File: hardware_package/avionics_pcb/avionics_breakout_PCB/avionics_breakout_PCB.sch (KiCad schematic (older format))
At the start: 5 parts, among them SW1 SW_Push

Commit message: Completed the PCB for the breakout board based avionics board. Also updated the CI/CD to include this new PCB
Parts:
- added J1: GPS, Connector_PinHeader_2.54mm:PinHeader_1x04_P2.54mm_Vertical, symbol Connector_Generic:Conn_01x04
- Barometer1: symbol avionics:MPL3115A2-Adafruit -> avionics_breakout_PCB-rescue:MPL3115A2-Adafruit-avionics
- IMU1: symbol avionics:MPU-6050-Adafruit -> avionics_breakout_PCB-rescue:MPU-6050-Adafruit-avionics
- LoRa_Radio1: symbol avionics:RFM98 -> avionics_breakout_PCB-rescue:RFM98-avionics
- STM32: symbol avionics:Adafruit_Feather_STM32F405 -> avionics_breakout_PCB-rescue:Adafruit_Feather_STM32F405-avionics
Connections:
- net GND: now also IMU1.7 (GND), LoRa_Radio1.16 (GND), LoRa_Radio1.2 (GND), LoRa_Radio1.9 (GND), J1.2 (Pin_2); no longer LoRa_Radio1.10 (GND)
- net CS: now reaches STM32.10 (A5)
- net CS: now also LoRa_Radio1.12 (NSS)
- net SCK: now reaches STM32.11 (SCK)
- net SCK: now also LoRa_Radio1.13 (SCK)
- net MOSI: now reaches STM32.12 (MO)
- net MOSI: now also LoRa_Radio1.14 (MOSI)
- net MISO: now reaches STM32.13 (MI)
- net MISO: now also LoRa_Radio1.15 (MISO)
- net RX: now reaches STM32.14 (RX)
- net RX: now also J1.4 (Pin_4)
- net TX: now reaches STM32.15 (TX)
- net TX: now also J1.3 (Pin_3)
- net INT_IMU: now reaches STM32.19 (5)
- net INT_IMU: now also IMU1.6 (INT)
- net RESET: now reaches STM32.20 (6)
- net RESET: now also LoRa_Radio1.11 (RESET)
- net INT_LORA: now reaches STM32.21 (9)
- net INT_LORA: now also LoRa_Radio1.6 (DIO0)
- net +3V3: now reaches LoRa_Radio1.5 (3V3)
- net +3V3: now also Barometer1.1 (VIN), IMU1.1 (VCC), STM32.2 (3V3), SW1.2, J1.1 (Pin_1)
- removed net 3V3: Barometer1.1 (VIN), IMU1.1 (VCC), LoRa_Radio1.13 (3V3), STM32.2 (3V3), STM32.3 (3V3), SW1.2
- no-connect marks 4 -> 29
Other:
- moved on the sheet: Barometer1, STM32, SW1

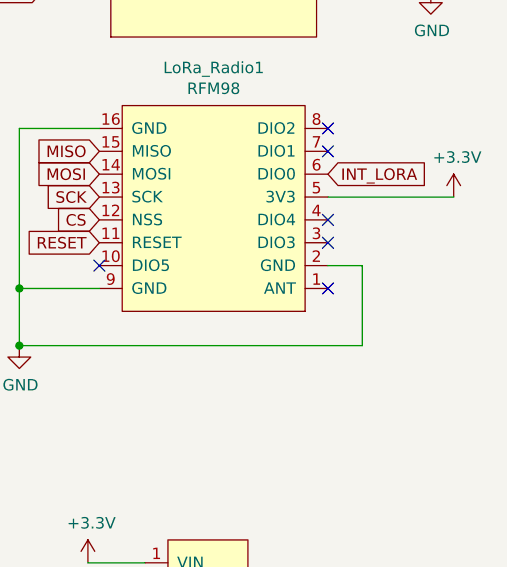
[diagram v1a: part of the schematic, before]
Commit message: Fixed DRC check errors
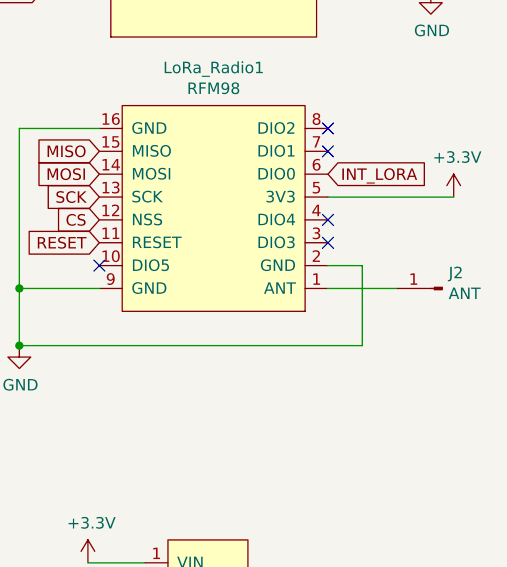
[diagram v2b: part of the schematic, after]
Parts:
- added J2: ANT, Connector_Wire:SolderWire-0.1sqmm_1x01_D0.4mm_OD1mm, symbol Connector:Conn_01x01_Male
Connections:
- net at LoRa_Radio1.1 (ANT): now also J2.1 (Pin_1)
- no-connect marks 29 -> 28
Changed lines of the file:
@@
 Wire Wire Line
 	8500 1500 8300 1500
-NoConn ~ 8050 2800
+$Comp
+L Connector:Conn_01x01_Male J2
+U 1 1 5F636A13
+P 8550 2800
+F 0 "J2" H 8522 2732 50  0000 R CNN
+F 1 "ANT" H 8522 2823 50  0000 R CNN
+F 2 "Connector_Wire:SolderWire-0.1sqmm_1x01_D0.4mm_OD1mm" H 8550 2800 50  0001 C CNN
+F 3 "~" H 8550 2800 50  0001 C CNN
+	1    8550 2800
+	-1   0    0    1
+$EndComp
+Wire Wire Line
+	8050 2800 8350 2800
 $EndSCHEMATC

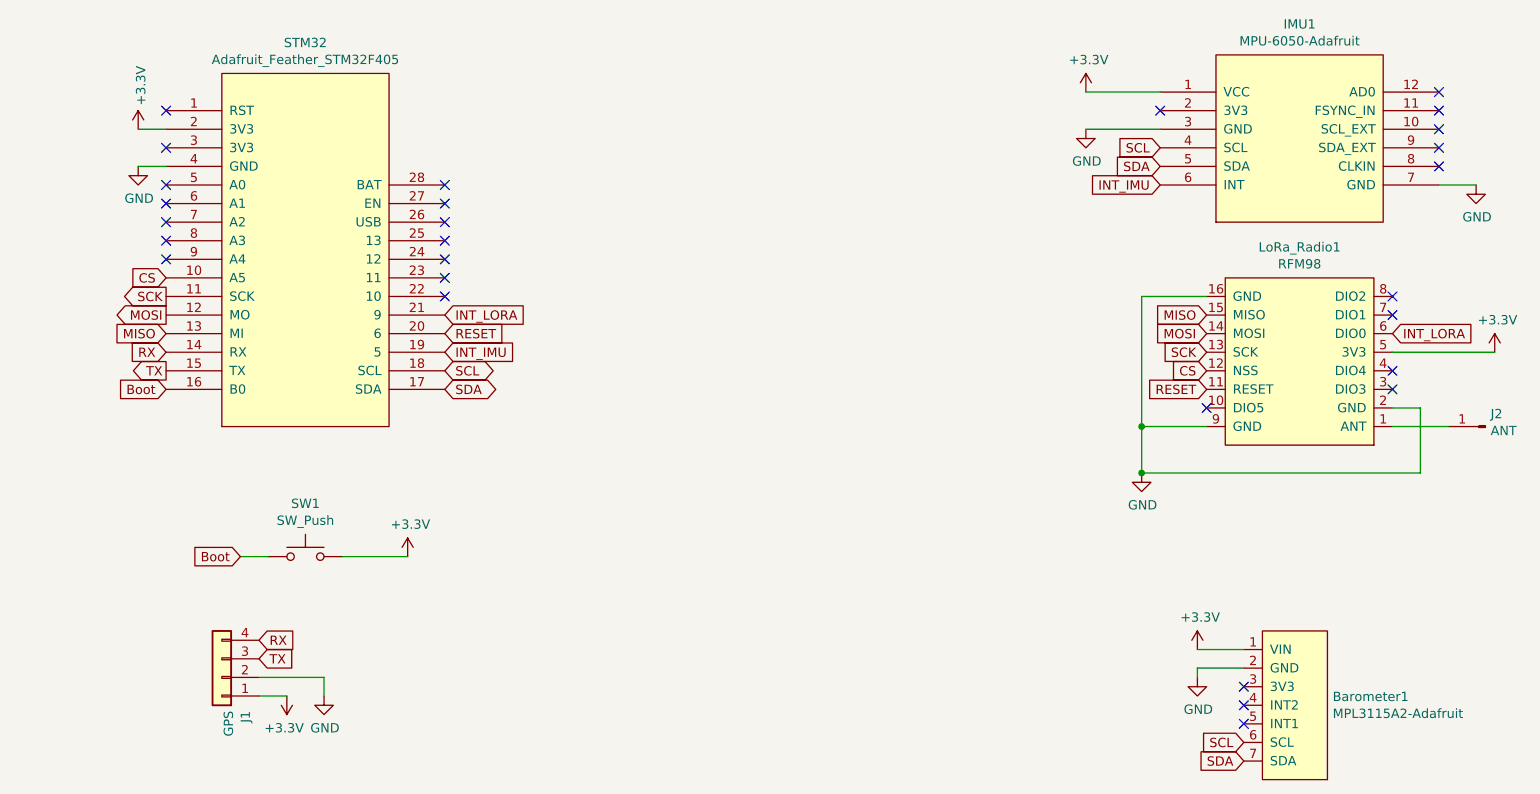
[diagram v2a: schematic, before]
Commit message: Added servo data connections, as well as ingnition charge data lines
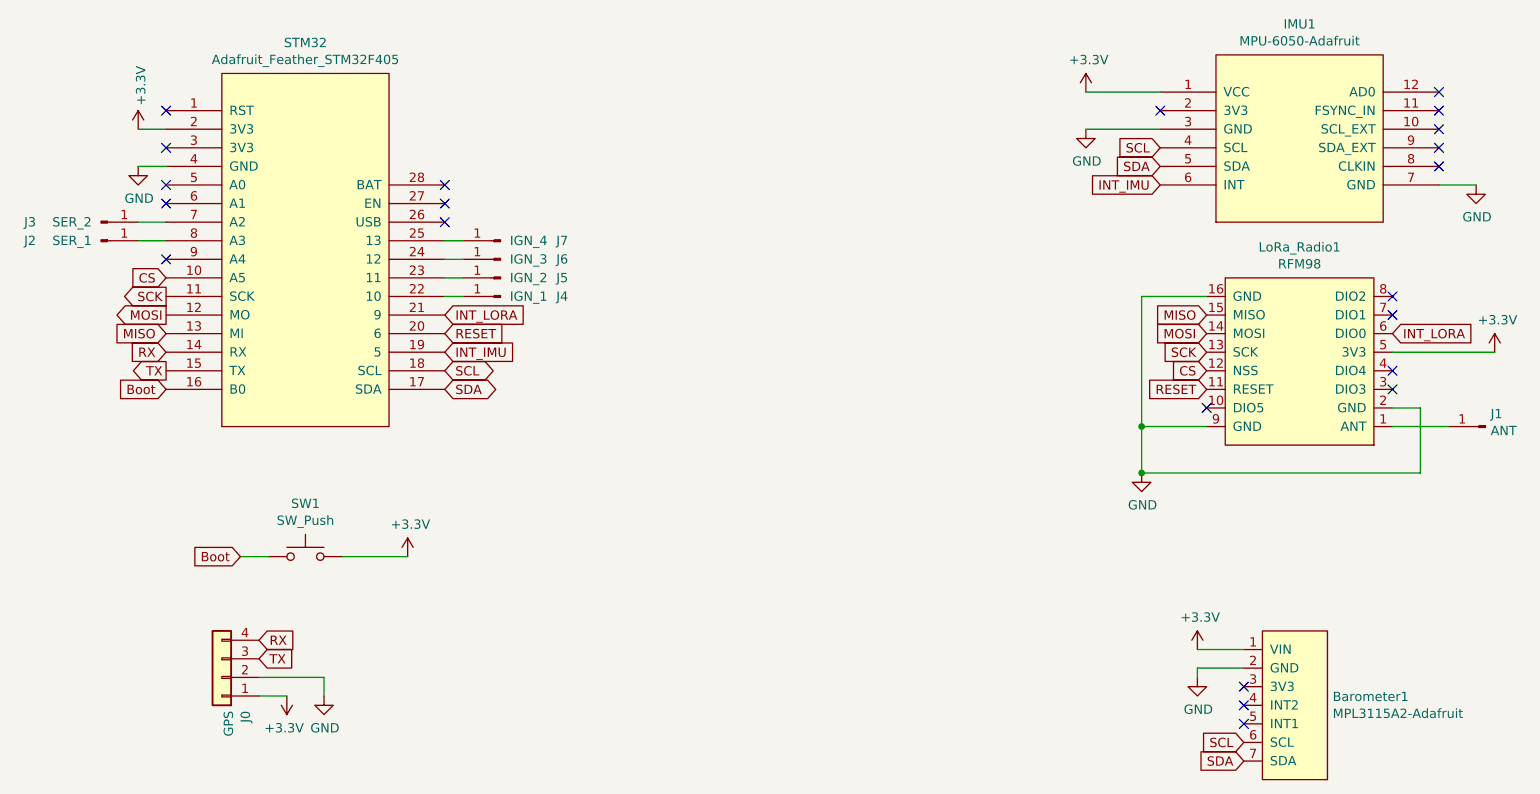
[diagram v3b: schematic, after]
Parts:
- added J2: SER_1, Connector_Wire:SolderWire-0.1sqmm_1x01_D0.4mm_OD1mm, symbol Connector:Conn_01x01_Male
- added J3: SER_2, Connector_Wire:SolderWire-0.1sqmm_1x01_D0.4mm_OD1mm, symbol Connector:Conn_01x01_Male
- added J4: IGN_1, Connector_Wire:SolderWire-0.1sqmm_1x01_D0.4mm_OD1mm, symbol Connector:Conn_01x01_Male
- added J5: IGN_2, Connector_Wire:SolderWire-0.1sqmm_1x01_D0.4mm_OD1mm, symbol Connector:Conn_01x01_Male
- added J6: IGN_3, Connector_Wire:SolderWire-0.1sqmm_1x01_D0.4mm_OD1mm, symbol Connector:Conn_01x01_Male
- added J7: IGN_4, Connector_Wire:SolderWire-0.1sqmm_1x01_D0.4mm_OD1mm, symbol Connector:Conn_01x01_Male
- renumbered J1 to J0, J2 to J1
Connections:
- net at STM32.22 (10): now also J4.1 (Pin_1)
- net at STM32.23 (11): now also J5.1 (Pin_1)
- net at STM32.24 (12): now also J6.1 (Pin_1)
- net at STM32.25 (13): now also J7.1 (Pin_1)
- net at STM32.7 (A2): now also J3.1 (Pin_1)
- net at STM32.8 (A3): now also J2.1 (Pin_1)
- no-connect marks 28 -> 22
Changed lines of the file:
@@
 Text GLabel 7050 2500 0    50   Input ~ 0
 CS
-Text GLabel 8050 2300 2    50   Input ~ 0
-INT_LORA
 Text GLabel 2950 2300 2    50   Input ~ 0
 RESET
@@
 NoConn ~ 1450 1500
 NoConn ~ 1450 1600
-NoConn ~ 1450 1700
-NoConn ~ 1450 1800
 NoConn ~ 1450 1900
 NoConn ~ 2950 1500
 NoConn ~ 2950 1600
 NoConn ~ 2950 1700
-NoConn ~ 2950 1800
-NoConn ~ 2950 1900
-NoConn ~ 2950 2000
-NoConn ~ 2950 2100
-$Comp
-L Connector_Generic:Conn_01x04 J1
+$Comp
+L Connector_Generic:Conn_01x04 J0
 U 1 1 5F64C92F
 P 1750 4150
-F 0 "J1" V 1622 4330 50  0000 L CNN
+F 0 "J0" V 1622 4330 50  0000 L CNN
 F 1 "GPS" V 1713 4330 50  0000 L CNN
 F 2 "Connector_PinHeader_2.54mm:PinHeader_1x04_P2.54mm_Vertical" H 1750 4150 50  0001 C CNN
@@
 Wire Wire Line
 	1300 1400 1450 1400
+NoConn ~ 1450 1300
+NoConn ~ 1450 1100
+Wire Wire Line
+	1300 1200 1450 1200
+$Comp
+L power:GND #PWR0105
+U 1 1 5F650983
+P 2300 4250
+F 0 "#PWR0105" H 2300 4000 50  0001 C CNN
+F 1 "GND" H 2305 4077 50  0000 C CNN
+F 2 "" H 2300 4250 50  0001 C CNN
+F 3 "" H 2300 4250 50  0001 C CNN
+	1    2300 4250
+	1    0    0    -1
+$EndComp
+$Comp
+L power:+3.3V #PWR0107
+U 1 1 5F661886
+P 2100 4250
+F 0 "#PWR0107" H 2100 4100 50  0001 C CNN
+F 1 "+3.3V" H 2115 4423 50  0000 C CNN
+F 2 "" H 2100 4250 50  0001 C CNN
+F 3 "" H 2100 4250 50  0001 C CNN
+	1    2100 4250
+	-1   0    0    1
+$EndComp
+Wire Wire Line
+	2300 4250 2300 4150
+Wire Wire Line
+	1950 4150 2300 4150
+Wire Wire Line
+	1950 4250 2100 4250
+$Comp
+L power:+3.3V #PWR0108
+U 1 1 5F66E8BF
+P 2750 3500
+F 0 "#PWR0108" H 2750 3350 50  0001 C CNN
+F 1 "+3.3V" H 2765 3673 50  0000 C CNN
+F 2 "" H 2750 3500 50  0001 C CNN
+F 3 "" H 2750 3500 50  0001 C CNN
+	1    2750 3500
+	1    0    0    -1
+$EndComp
+Wire Wire Line
+	2400 3500 2750 3500
+$Comp
+L power:+3.3V #PWR0109
+U 1 1 5F66F707
+P 6400 1000
+F 0 "#PWR0109" H 6400 850 50  0001 C CNN
+F 1 "+3.3V" H 6415 1173 50  0000 C CNN
+F 2 "" H 6400 1000 50  0001 C CNN
+F 3 "" H 6400 1000 50  0001 C CNN
+	1    6400 1000
+	1    0    0    -1
+$EndComp
+Wire Wire Line
+	6400 1000 6800 1000
+$Comp
+L power:+3.3V #PWR0110
+U 1 1 5F67048B
+P 8600 2400
+F 0 "#PWR0110" H 8600 2250 50  0001 C CNN
+F 1 "+3.3V" H 8615 2573 50  0000 C CNN
+F 2 "" H 8600 2400 50  0001 C CNN
+F 3 "" H 8600 2400 50  0001 C CNN
+	1    8600 2400
+	1    0    0    -1
+$EndComp
+Wire Wire Line
+	8600 2400 8050 2400
+$Comp
+L power:+3.3V #PWR0111
+U 1 1 5F671090
+P 7000 4000
+F 0 "#PWR0111" H 7000 3850 50  0001 C CNN
+F 1 "+3.3V" H 7015 4173 50  0000 C CNN
+F 2 "" H 7000 4000 50  0001 C CNN
+F 3 "" H 7000 4000 50  0001 C CNN
+	1    7000 4000
+	1    0    0    -1
+$EndComp
+Wire Wire Line
+	7000 4000 7250 4000
+$Comp
+L power:GND #PWR0112
+U 1 1 5F67C4FF
+P 8500 1500
+F 0 "#PWR0112" H 8500 1250 50  0001 C CNN
+F 1 "GND" H 8505 1327 50  0000 C CNN
+F 2 "" H 8500 1500 50  0001 C CNN
+F 3 "" H 8500 1500 50  0001 C CNN
+	1    8500 1500
+	1    0    0    -1
+$EndComp
+Wire Wire Line
+	8500 1500 8300 1500
+$Comp
+L Connector:Conn_01x01_Male J1
+U 1 1 5F636A13
+P 8550 2800
+F 0 "J1" H 8522 2732 50  0000 R CNN
+F 1 "ANT" H 8522 2823 50  0000 R CNN
+F 2 "Connector_Wire:SolderWire-0.1sqmm_1x01_D0.4mm_OD1mm" H 8550 2800 50  0001 C CNN
+F 3 "~" H 8550 2800 50  0001 C CNN
+	1    8550 2800
+	-1   0    0    1
+$EndComp
+Wire Wire Line
+	8050 2800 8350 2800
+Text GLabel 8050 2300 2    50   Input ~ 0
+INT_LORA
 $Comp
 L avionics_breakout_PCB-rescue:Adafruit_Feather_STM32F405-avionics STM32
@@
 	1    0    0    -1
 $EndComp
-NoConn ~ 1450 1300
-NoConn ~ 1450 1100
-Wire Wire Line
-	1300 1200 1450 1200
-$Comp
-L power:GND #PWR0105
-U 1 1 5F650983
-P 2300 4250
-F 0 "#PWR0105" H 2300 4000 50  0001 C CNN
-F 1 "GND" H 2305 4077 50  0000 C CNN
-F 2 "" H 2300 4250 50  0001 C CNN
-F 3 "" H 2300 4250 50  0001 C CNN
-	1    2300 4250
-	1    0    0    -1
-$EndComp
-$Comp
-L power:+3.3V #PWR0107
-U 1 1 5F661886
-P 2100 4250
-F 0 "#PWR0107" H 2100 4100 50  0001 C CNN
-F 1 "+3.3V" H 2115 4423 50  0000 C CNN
-F 2 "" H 2100 4250 50  0001 C CNN
-F 3 "" H 2100 4250 50  0001 C CNN
-	1    2100 4250
-	-1   0    0    1
-$EndComp
-Wire Wire Line
-	2300 4250 2300 4150
-Wire Wire Line
-	1950 4150 2300 4150
-Wire Wire Line
-	1950 4250 2100 4250
-$Comp
-L power:+3.3V #PWR0108
-U 1 1 5F66E8BF
-P 2750 3500
-F 0 "#PWR0108" H 2750 3350 50  0001 C CNN
-F 1 "+3.3V" H 2765 3673 50  0000 C CNN
-F 2 "" H 2750 3500 50  0001 C CNN
-F 3 "" H 2750 3500 50  0001 C CNN
-	1    2750 3500
-	1    0    0    -1
-$EndComp
-Wire Wire Line
-	2400 3500 2750 3500
-$Comp
-L power:+3.3V #PWR0109
-U 1 1 5F66F707
-P 6400 1000
-F 0 "#PWR0109" H 6400 850 50  0001 C CNN
-F 1 "+3.3V" H 6415 1173 50  0000 C CNN
-F 2 "" H 6400 1000 50  0001 C CNN
-F 3 "" H 6400 1000 50  0001 C CNN
-	1    6400 1000
-	1    0    0    -1
-$EndComp
-Wire Wire Line
-	6400 1000 6800 1000
-$Comp
-L power:+3.3V #PWR0110
-U 1 1 5F67048B
-P 8600 2400
-F 0 "#PWR0110" H 8600 2250 50  0001 C CNN
-F 1 "+3.3V" H 8615 2573 50  0000 C CNN
-F 2 "" H 8600 2400 50  0001 C CNN
-F 3 "" H 8600 2400 50  0001 C CNN
-	1    8600 2400
-	1    0    0    -1
-$EndComp
-Wire Wire Line
-	8600 2400 8050 2400
-$Comp
-L power:+3.3V #PWR0111
-U 1 1 5F671090
-P 7000 4000
-F 0 "#PWR0111" H 7000 3850 50  0001 C CNN
-F 1 "+3.3V" H 7015 4173 50  0000 C CNN
-F 2 "" H 7000 4000 50  0001 C CNN
-F 3 "" H 7000 4000 50  0001 C CNN
-	1    7000 4000
-	1    0    0    -1
-$EndComp
-Wire Wire Line
-	7000 4000 7250 4000
-$Comp
-L power:GND #PWR0112
-U 1 1 5F67C4FF
-P 8500 1500
-F 0 "#PWR0112" H 8500 1250 50  0001 C CNN
-F 1 "GND" H 8505 1327 50  0000 C CNN
-F 2 "" H 8500 1500 50  0001 C CNN
-F 3 "" H 8500 1500 50  0001 C CNN
-	1    8500 1500
-	1    0    0    -1
-$EndComp
-Wire Wire Line
-	8500 1500 8300 1500
+$Comp
+L Connector:Conn_01x01_Male J3
+U 1 1 5F65726D
+P 1100 1700
+F 0 "J3" H 750 1700 50  0000 R CNN
+F 1 "SER_2" H 1050 1700 50  0000 R CNN
+F 2 "Connector_Wire:SolderWire-0.1sqmm_1x01_D0.4mm_OD1mm" H 1100 1700 50  0001 C CNN
+F 3 "~" H 1100 1700 50  0001 C CNN
+	1    1100 1700
+	1    0    0    -1
+$EndComp
 $Comp
 L Connector:Conn_01x01_Male J2
-U 1 1 5F636A13
-P 8550 2800
-F 0 "J2" H 8522 2732 50  0000 R CNN
-F 1 "ANT" H 8522 2823 50  0000 R CNN
-F 2 "Connector_Wire:SolderWire-0.1sqmm_1x01_D0.4mm_OD1mm" H 8550 2800 50  0001 C CNN
-F 3 "~" H 8550 2800 50  0001 C CNN
-	1    8550 2800
-	-1   0    0    1
-$EndComp
-Wire Wire Line
-	8050 2800 8350 2800
+U 1 1 5F658B0B
+P 1100 1800
+F 0 "J2" H 750 1800 50  0000 R CNN
+F 1 "SER_1" H 1050 1800 50  0000 R CNN
+F 2 "Connector_Wire:SolderWire-0.1sqmm_1x01_D0.4mm_OD1mm" H 1100 1800 50  0001 C CNN
+F 3 "~" H 1100 1800 50  0001 C CNN
+	1    1100 1800
+	1    0    0    -1
+$EndComp
+Wire Wire Line
+	1300 1700 1450 1700
+Wire Wire Line
+	1300 1800 1450 1800
+$Comp
+L Connector:Conn_01x01_Male J4
+U 1 1 5F65C68E
+P 3250 2100
+F 0 "J4" H 2950 2100 50  0000 R CNN
+F 1 "IGN_1" H 3200 2100 50  0000 R CNN
+F 2 "Connector_Wire:SolderWire-0.1sqmm_1x01_D0.4mm_OD1mm" H 3250 2100 50  0001 C CNN
+F 3 "~" H 3250 2100 50  0001 C CNN
+	1    3250 2100
+	-1   0    0    1
+$EndComp
+$Comp
+L Connector:Conn_01x01_Male J5
+U 1 1 5F65D9FC
+P 3250 2000
+F 0 "J5" H 2950 2000 50  0000 R CNN
+F 1 "IGN_2" H 3200 2000 50  0000 R CNN
+F 2 "Connector_Wire:SolderWire-0.1sqmm_1x01_D0.4mm_OD1mm" H 3250 2000 50  0001 C CNN
+F 3 "~" H 3250 2000 50  0001 C CNN
+	1    3250 2000
+	-1   0    0    1
+$EndComp
+$Comp
+L Connector:Conn_01x01_Male J6
+U 1 1 5F65DEA0
+P 3250 1900
+F 0 "J6" H 2950 1900 50  0000 R CNN
+F 1 "IGN_3" H 3200 1900 50  0000 R CNN
+F 2 "Connector_Wire:SolderWire-0.1sqmm_1x01_D0.4mm_OD1mm" H 3250 1900 50  0001 C CNN
+F 3 "~" H 3250 1900 50  0001 C CNN
+	1    3250 1900
+	-1   0    0    1
+$EndComp
+$Comp
+L Connector:Conn_01x01_Male J7
+U 1 1 5F65E280
+P 3250 1800
+F 0 "J7" H 2950 1800 50  0000 R CNN
+F 1 "IGN_4" H 3200 1800 50  0000 R CNN
+F 2 "Connector_Wire:SolderWire-0.1sqmm_1x01_D0.4mm_OD1mm" H 3250 1800 50  0001 C CNN
+F 3 "~" H 3250 1800 50  0001 C CNN
+	1    3250 1800
+	-1   0    0    1
+$EndComp
+Wire Wire Line
+	2950 1800 3050 1800
+Wire Wire Line
+	2950 1900 3050 1900
+Wire Wire Line
+	2950 2000 3050 2000
+Wire Wire Line
+	2950 2100 3050 2100
 $EndSCHEMATC

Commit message: Finalised the breakout board PCB
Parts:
- added J8: 3V3_IN, Connector_Wire:SolderWire-0.1sqmm_1x01_D0.4mm_OD1mm, symbol Connector:Conn_01x01_Male
- added J9: GND_IN, Connector_Wire:SolderWire-0.1sqmm_1x01_D0.4mm_OD1mm, symbol Connector:Conn_01x01_Male
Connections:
- net +3V3: now also J8.1 (Pin_1)
- net GND: now also J9.1 (Pin_1)
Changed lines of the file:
@@
 Wire Wire Line
 	1300 1400 1450 1400
-NoConn ~ 1450 1300
 NoConn ~ 1450 1100
 Wire Wire Line
@@
 Wire Wire Line
 	2950 2100 3050 2100
+$Comp
+L Connector:Conn_01x01_Male J9
+U 1 1 5F646CDC
+P 1100 1400
+F 0 "J9" H 750 1400 50  0000 R CNN
+F 1 "GND_IN" H 1050 1400 50  0000 R CNN
+F 2 "Connector_Wire:SolderWire-0.1sqmm_1x01_D0.4mm_OD1mm" H 1100 1400 50  0001 C CNN
+F 3 "~" H 1100 1400 50  0001 C CNN
+	1    1100 1400
+	1    0    0    -1
+$EndComp
+$Comp
+L Connector:Conn_01x01_Male J8
+U 1 1 5F649BF1
+P 1100 1200
+F 0 "J8" H 750 1200 50  0000 R CNN
+F 1 "3V3_IN" H 1050 1200 50  0000 R CNN
+F 2 "Connector_Wire:SolderWire-0.1sqmm_1x01_D0.4mm_OD1mm" H 1100 1200 50  0001 C CNN
+F 3 "~" H 1100 1200 50  0001 C CNN
+	1    1100 1200
+	1    0    0    -1
+$EndComp
+NoConn ~ 1450 1300
 $EndSCHEMATC
